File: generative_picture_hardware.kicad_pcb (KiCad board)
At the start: 2 copper layers, 100 x 100 mm, 64 parts, among them J1 e_Paper_HAT, J2 Conn_ARM_JTAG_SWD_10, J3 USB_C_Receptacle_USB2.0, Q1 PMN48XP, Q2 DMG9926UDM, Q3 MBT3904DW1, SW1 SW_Push, SW2 SW_Push, U1 AP2112K-3.3, U2 ESP32-WROOM-32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

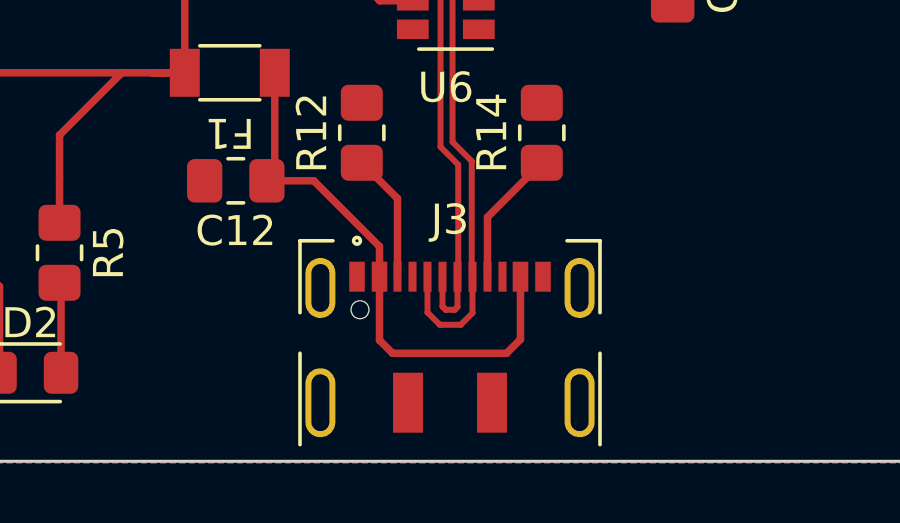
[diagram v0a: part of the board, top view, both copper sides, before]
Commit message: Fixes clearance between Vbus track and usb connector mounting hole
This will probably need to be reworked once I increase the thickness for
the power lines.
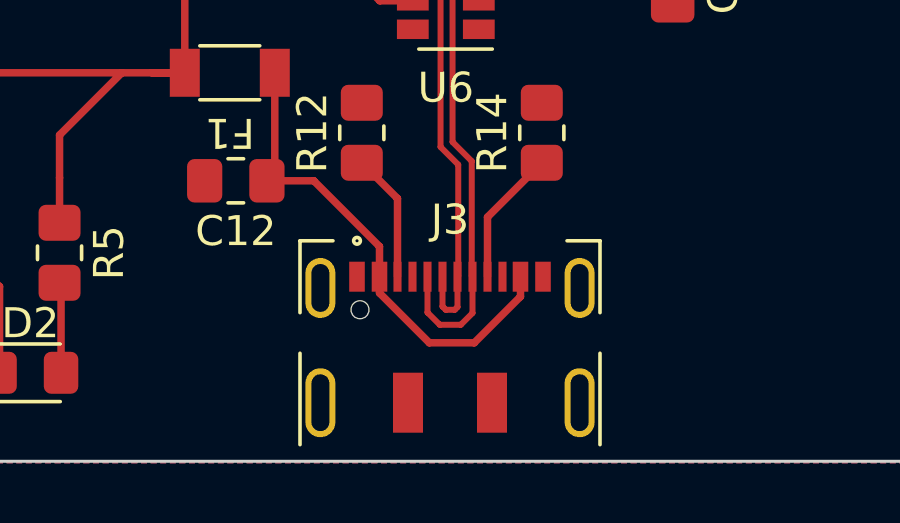
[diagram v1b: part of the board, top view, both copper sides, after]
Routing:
- net Net-(C12-Pad1): track 18.7 -> 16.6 mm
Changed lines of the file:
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@@
     (fp_line (start -1 0.6) (end 1 0.6) (layer "F.Fab") (width 0.1))
     (pad "1" smd roundrect (at -1.025 0 180) (locked) (size 1.15 1.4) (layers "F.Cu" "F.Paste" "F.Mask") (roundrect_rratio 0.217391)
-      (net 3 "GND") (pinfunction "K") (pintype "passive"))
+      (net 3 "GND") (pinfunction "K"))
     (pad "2" smd roundrect (at 1.025 0 180) (locked) (size 1.15 1.4) (layers "F.Cu" "F.Paste" "F.Mask") (roundrect_rratio 0.217391)
-      (net 17 "Net-(D3-Pad2)") (pinfunction "A") (pintype "passive"))
+      (net 17 "Net-(D3-Pad2)") (pinfunction "A"))
     (model "${KISYS3DMOD}/LED_SMD.3dshapes/LED_0805_2012Metric.wrl"
       (offset (xyz 0 0 0))
@@
   (segment (start 140 139) (end 141.1 139) (width 0.25) (layer "F.Cu") (net 9))
   (segment (start 141.1 131.9) (end 143.5 129.5) (width 0.25) (layer "F.Cu") (net 9))
+  (segment (start 150.75 148) (end 152.29 146.46) (width 0.25) (layer "F.Cu") (net 10))
   (segment (start 145.4 142.6) (end 147.59 144.79) (width 0.25) (layer "F.Cu") (net 10))
-  (segment (start 147.59 145.7975) (end 147.59 147.915) (width 0.25) (layer "F.Cu") (net 10))
   (segment (start 144.1 139) (end 144.1 142.3375) (width 0.25) (layer "F.Cu") (net 10))
+  (segment (start 149.25 148) (end 150.75 148) (width 0.25) (layer "F.Cu") (net 10))
   (segment (start 144.1 142.3375) (end 143.8375 142.6) (width 0.25) (layer "F.Cu") (net 10))
-  (segment (start 151.825 148.35) (end 152.29 147.885) (width 0.25) (layer "F.Cu") (net 10))
   (segment (start 147.59 144.79) (end 147.59 145.7975) (width 0.25) (layer "F.Cu") (net 10))
-  (segment (start 148.025 148.35) (end 151.825 148.35) (width 0.25) (layer "F.Cu") (net 10))
-  (segment (start 147.59 147.915) (end 148.025 148.35) (width 0.25) (layer "F.Cu") (net 10))
+  (segment (start 152.29 146.46) (end 152.29 145.7975) (width 0.25) (layer "F.Cu") (net 10))
   (segment (start 143.8375 142.6) (end 145.4 142.6) (width 0.25) (layer "F.Cu") (net 10))
-  (segment (start 152.29 147.885) (end 152.29 145.7975) (width 0.25) (layer "F.Cu") (net 10))
+  (segment (start 147.59 145.7975) (end 147.59 146.34) (width 0.25) (layer "F.Cu") (net 10))
+  (segment (start 147.59 146.34) (end 149.25 148) (width 0.25) (layer "F.Cu") (net 10))
   (segment (start 156 67.0375) (end 160.5 67.0375) (width 0.25) (layer "F.Cu") (net 11))
   (segment (start 161 66.5375) (end 161 65.9) (width 0.25) (layer "F.Cu") (net 11))

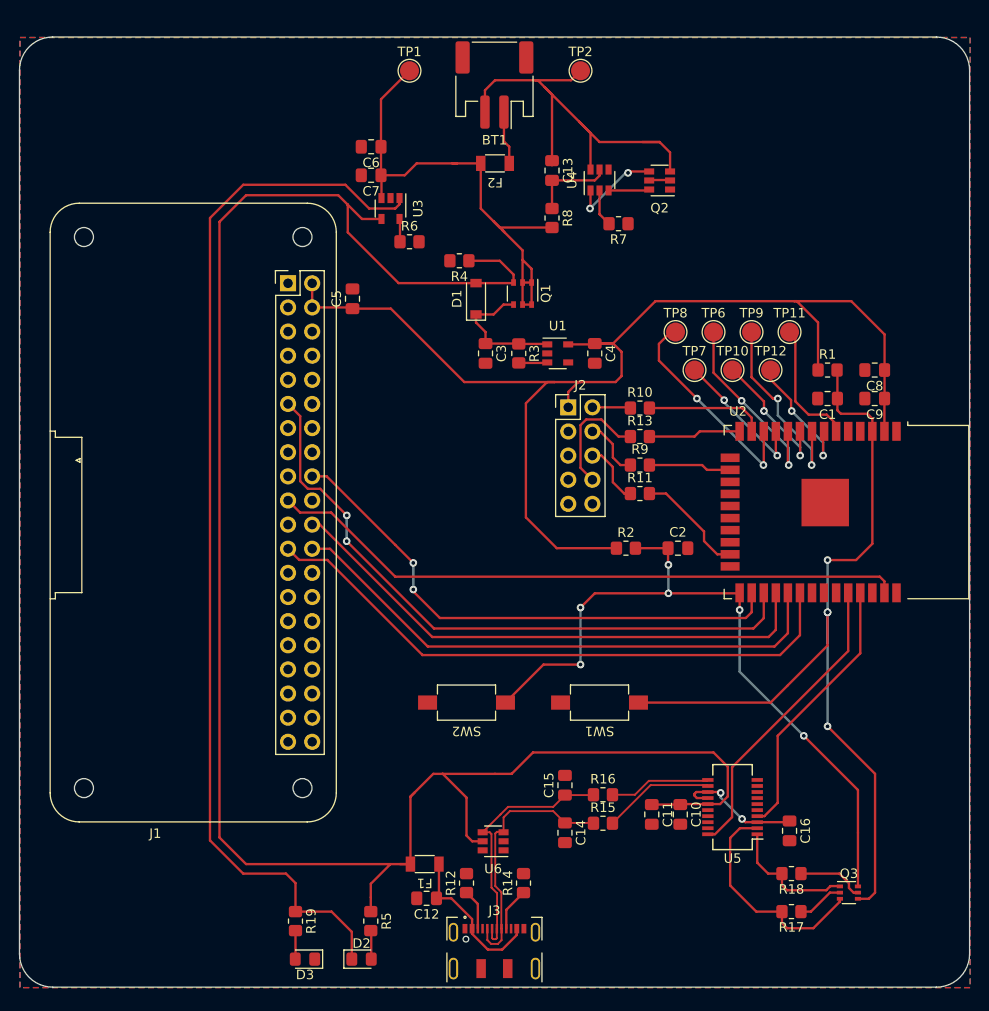
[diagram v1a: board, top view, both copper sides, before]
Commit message: Routes all ground without relying on the top copper fill
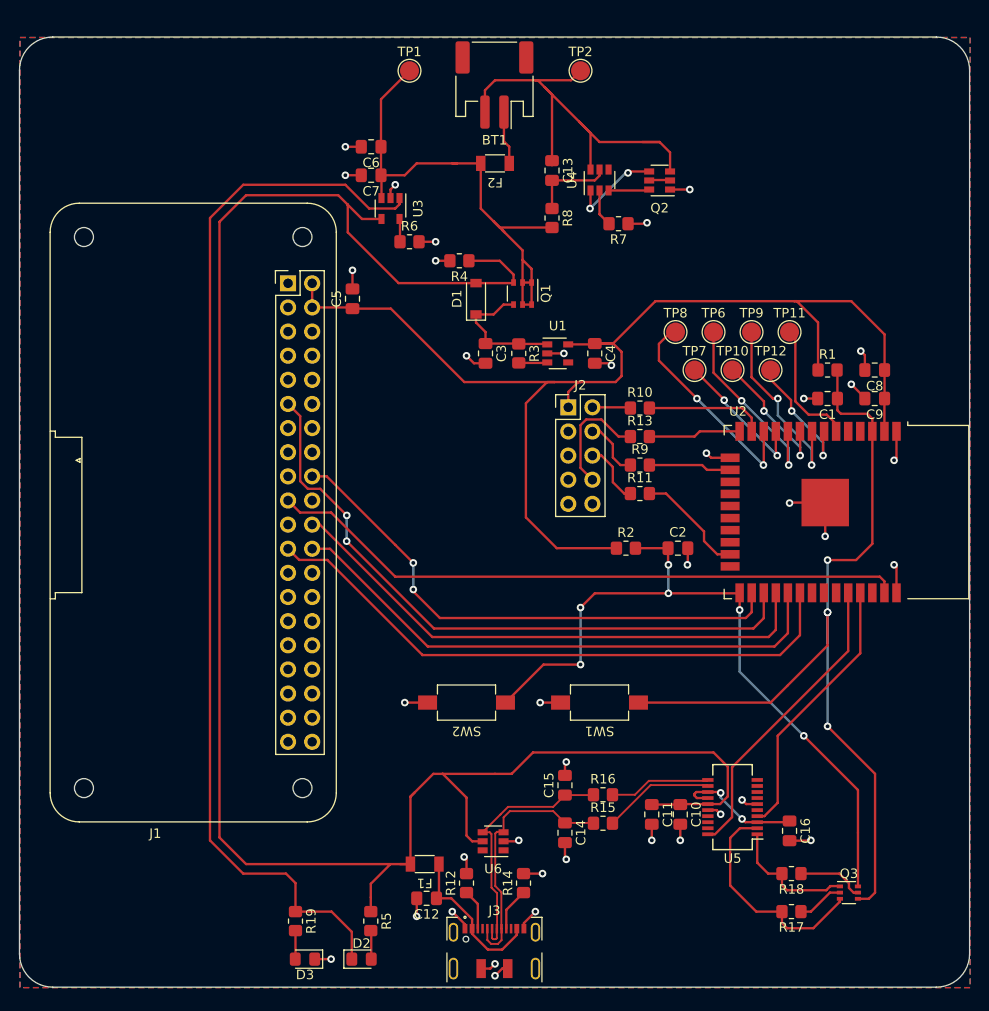
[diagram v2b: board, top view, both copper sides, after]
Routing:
- net GND: track 0.00 -> 77.8 mm, vias 0 -> 38

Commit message: Deletes all tracks and (very) roughly repositions groups of components
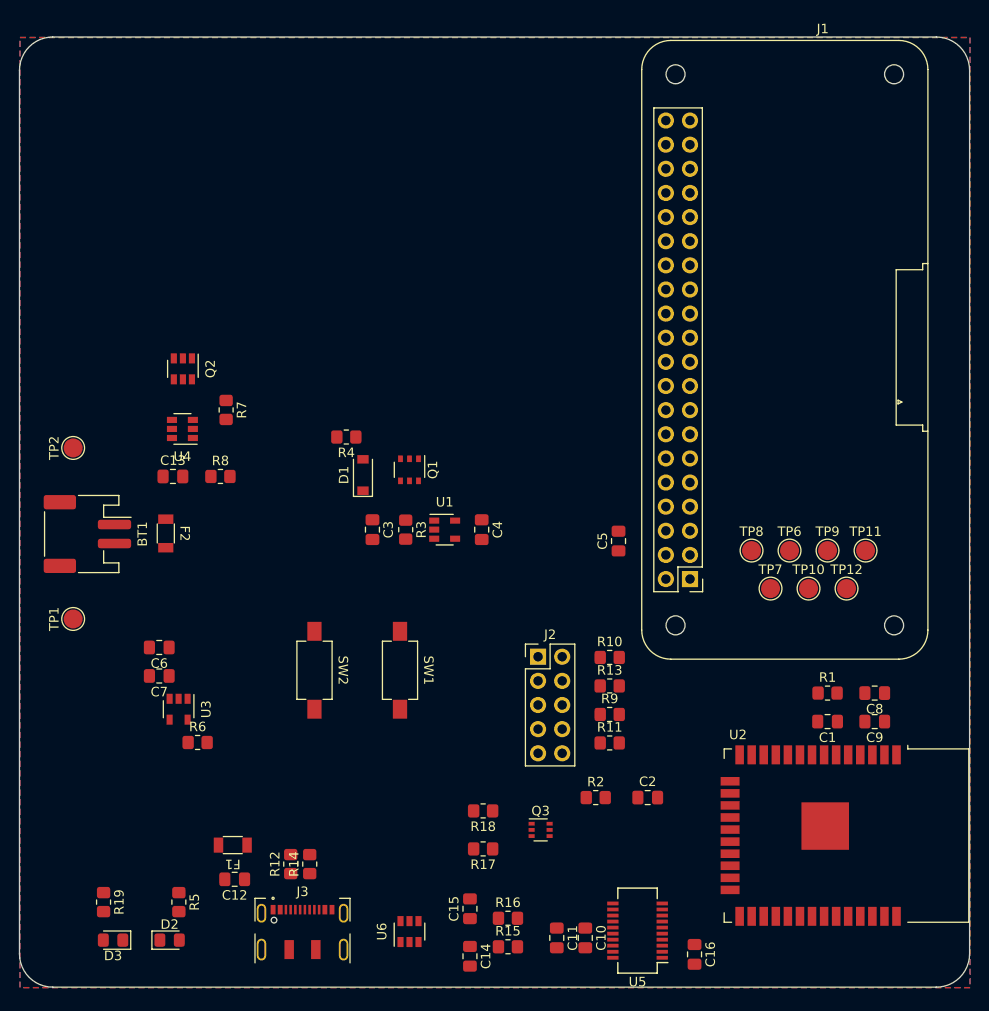
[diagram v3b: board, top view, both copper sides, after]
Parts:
- moved TP1 67.7 mm to (105.6, 113.2), turned to 90 degrees
- moved TP2 66.5 mm to (105.6, 95.2), turned to 90 degrees
- moved BT1 63.8 mm to (107.1, 104.3), turned to -90 degrees
- moved C6 57.2 mm to (114.7, 116.2)
- moved C7 57.2 mm to (114.7, 119.2)
- moved R6 57.2 mm to (118.7, 126.2)
- moved U3 57.2 mm to (116.7, 122.7)
- moved Q2 53.9 mm to (117.2, 86.9), turned to -90 degrees
- moved J1 52.5 mm to (170.5, 109.0), turned to 180 degrees
- moved F2 52.1 mm to (115.3, 104.2), turned to -90 degrees
- moved C13 51.3 mm to (116.1, 98.2), turned to 0 degrees
- moved U4 51.1 mm to (117.1, 93.2), turned to 180 degrees
- moved R7 45.7 mm to (121.7, 91.2), turned to -90 degrees
- moved R8 44.2 mm to (121.1, 98.2), turned to 0 degrees
- moved C5 37.9 mm to (163.0, 105.0)
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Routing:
- net +5V: track 206.0 -> 0.00 mm
- net +3V3: track 129.8 -> 0.00 mm
- net Net-(D2-Pad1): track 112.3 -> 0.00 mm
- net ESP_EN: track 91.9 -> 0.00 mm, vias 4 -> 0
- net GND: track 77.8 -> 0.00 mm, vias 38 -> 0
- net ESP_BOOT: track 77.2 -> 0.00 mm, vias 6 -> 0
- net EPD_RST: track 68.6 -> 0.00 mm, vias 2 -> 0
- net EPD_DIN: track 67.5 -> 0.00 mm
- net EPD_CLK: track 63.9 -> 0.00 mm
- net EPD_CS: track 59.2 -> 0.00 mm
- net EPD_DC: track 57.9 -> 0.00 mm
- net +BATT: track 56.6 -> 0.00 mm
- net EPD_BUSY: track 56.5 -> 0.00 mm, vias 2 -> 0
- net Net-(BT1-Pad2): track 48.3 -> 0.00 mm
- net ESP_RX: track 32.0 -> 0.00 mm
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
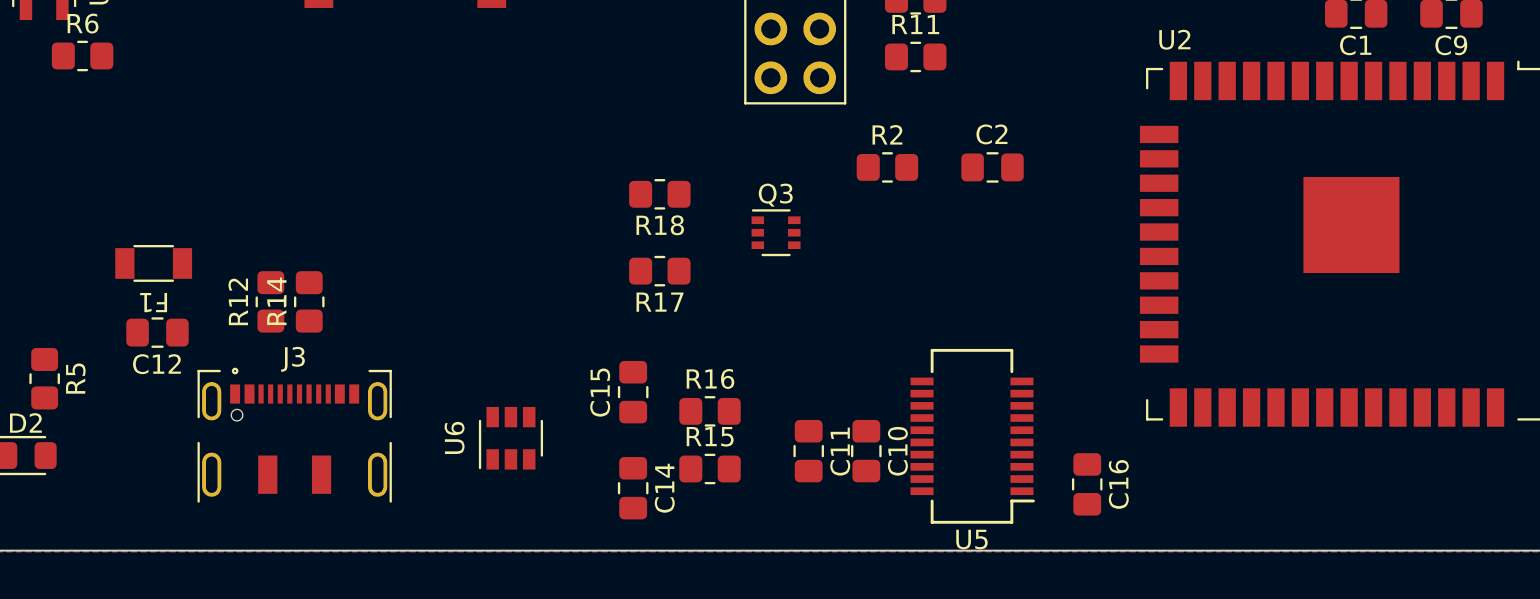
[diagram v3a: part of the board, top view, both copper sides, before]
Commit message: Routes USB to UART
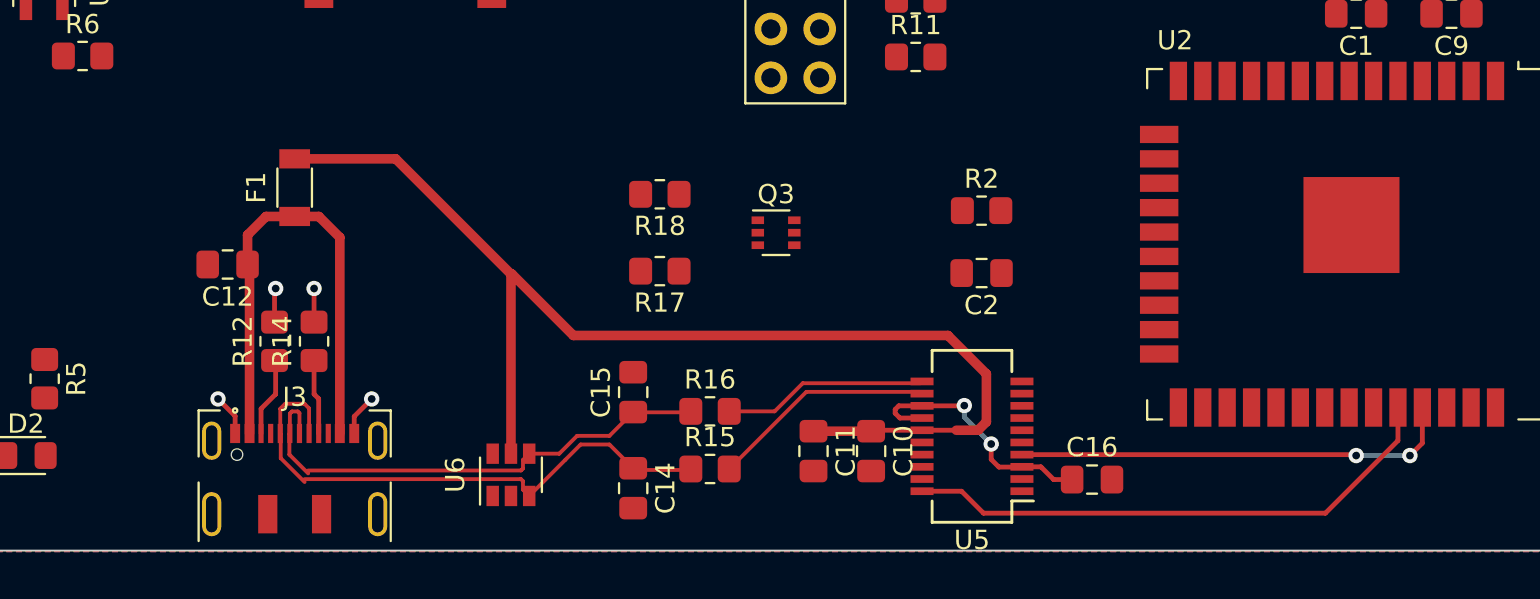
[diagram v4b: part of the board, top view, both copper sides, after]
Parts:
- moved F1 8.33 mm to (129.7, 133.1), turned to 90 degrees
- moved C2 5.53 mm to (165.5, 137.5), turned to 180 degrees
- moved R2 5.39 mm to (165.5, 134.2)
- moved C12 5.09 mm to (126.2, 137.1)
- moved R14 2.07 mm to (130.8, 141.1)
- moved R12 2.06 mm to (128.7, 141.1)
- moved J3 2.05 mm to (129.7, 148.2)
- moved U6 1.90 mm to (141.0, 148.0)
- moved C16 0.35 mm to (171.2, 148.2), turned to 0 degrees
- moved C10 0.25 mm to (159.8, 146.8)
- moved C11 0.25 mm to (156.8, 146.8)
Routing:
- net +5V: track 0.00 -> 61.8 mm
- net /D-: track 0.00 -> 29.8 mm
- net ESP_RX: track 0.00 -> 28.5 mm
- net /D+: track 0.00 -> 26.6 mm
- net Net-(C12-Pad1): track 0.00 -> 26.2 mm
- net ESP_TX: track 0.00 -> 23.0 mm, vias 0 -> 2
- net Net-(C16-Pad1): track 0.00 -> 13.4 mm, vias 0 -> 2
- net /USBD-: track 0.00 -> 11.7 mm
- net /USBD+: track 0.00 -> 10.7 mm
- net GND: track 0.00 -> 7.86 mm, vias 0 -> 4
- net Net-(J3-PadA5): track 0.00 -> 4.14 mm
- net Net-(J3-PadB5): track 0.00 -> 3.90 mm
